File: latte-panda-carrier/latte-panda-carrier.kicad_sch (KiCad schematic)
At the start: 6 parts

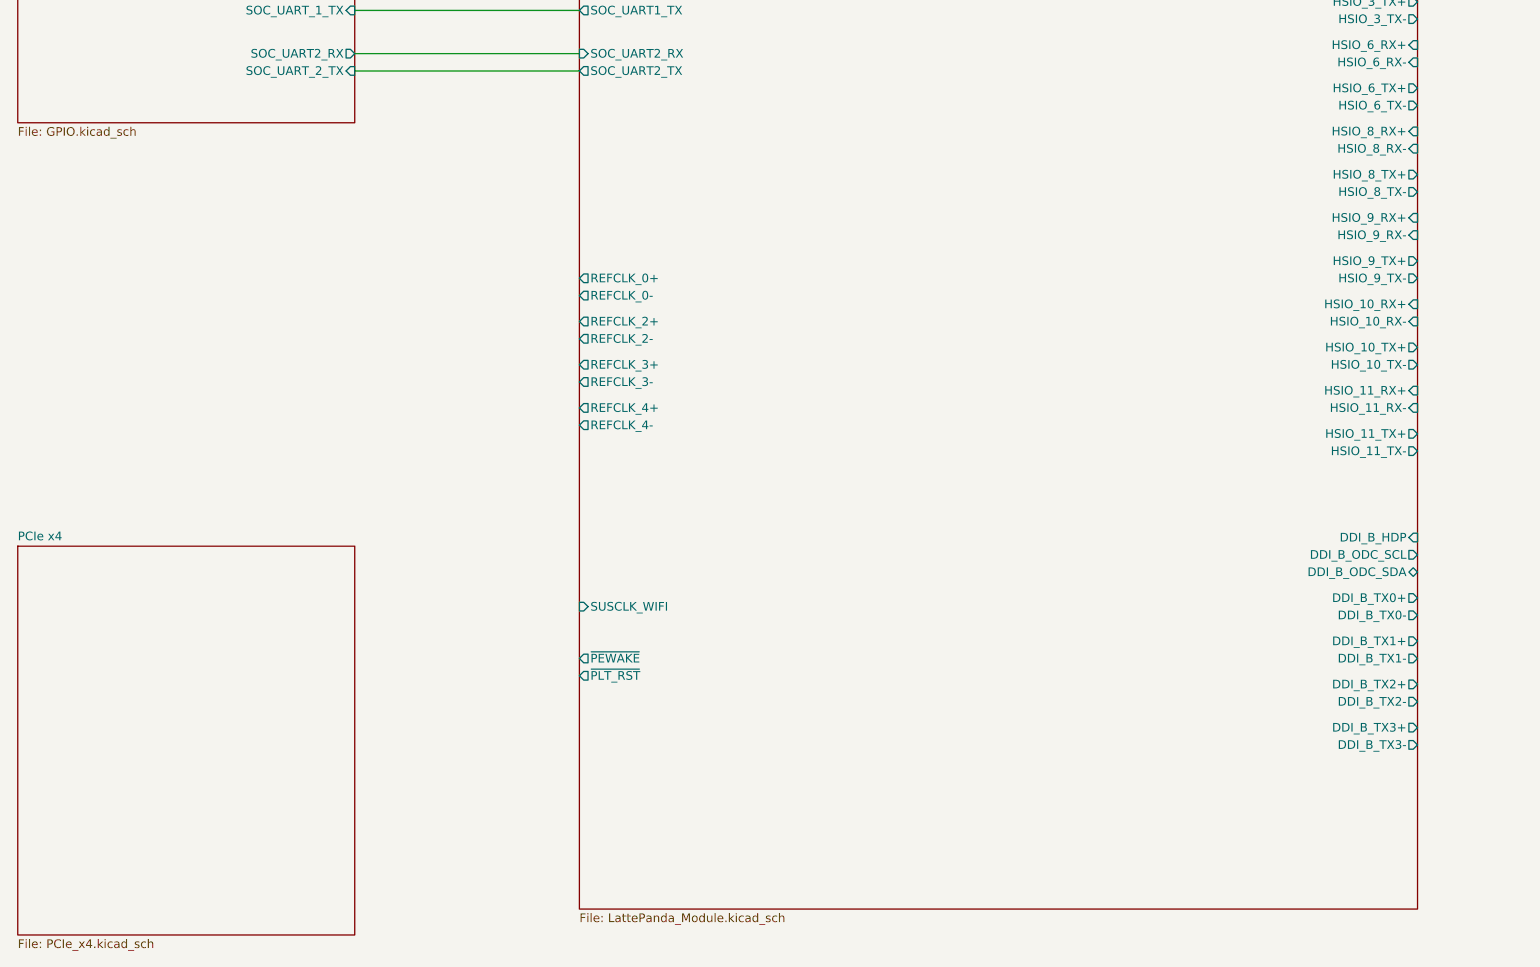
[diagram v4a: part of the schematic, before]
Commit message: 140.2
Add PCIe x4 connector. Instructor left one ERC problem, but I left it
unresolved, as ignored with a comment, as the course will not be routing it.
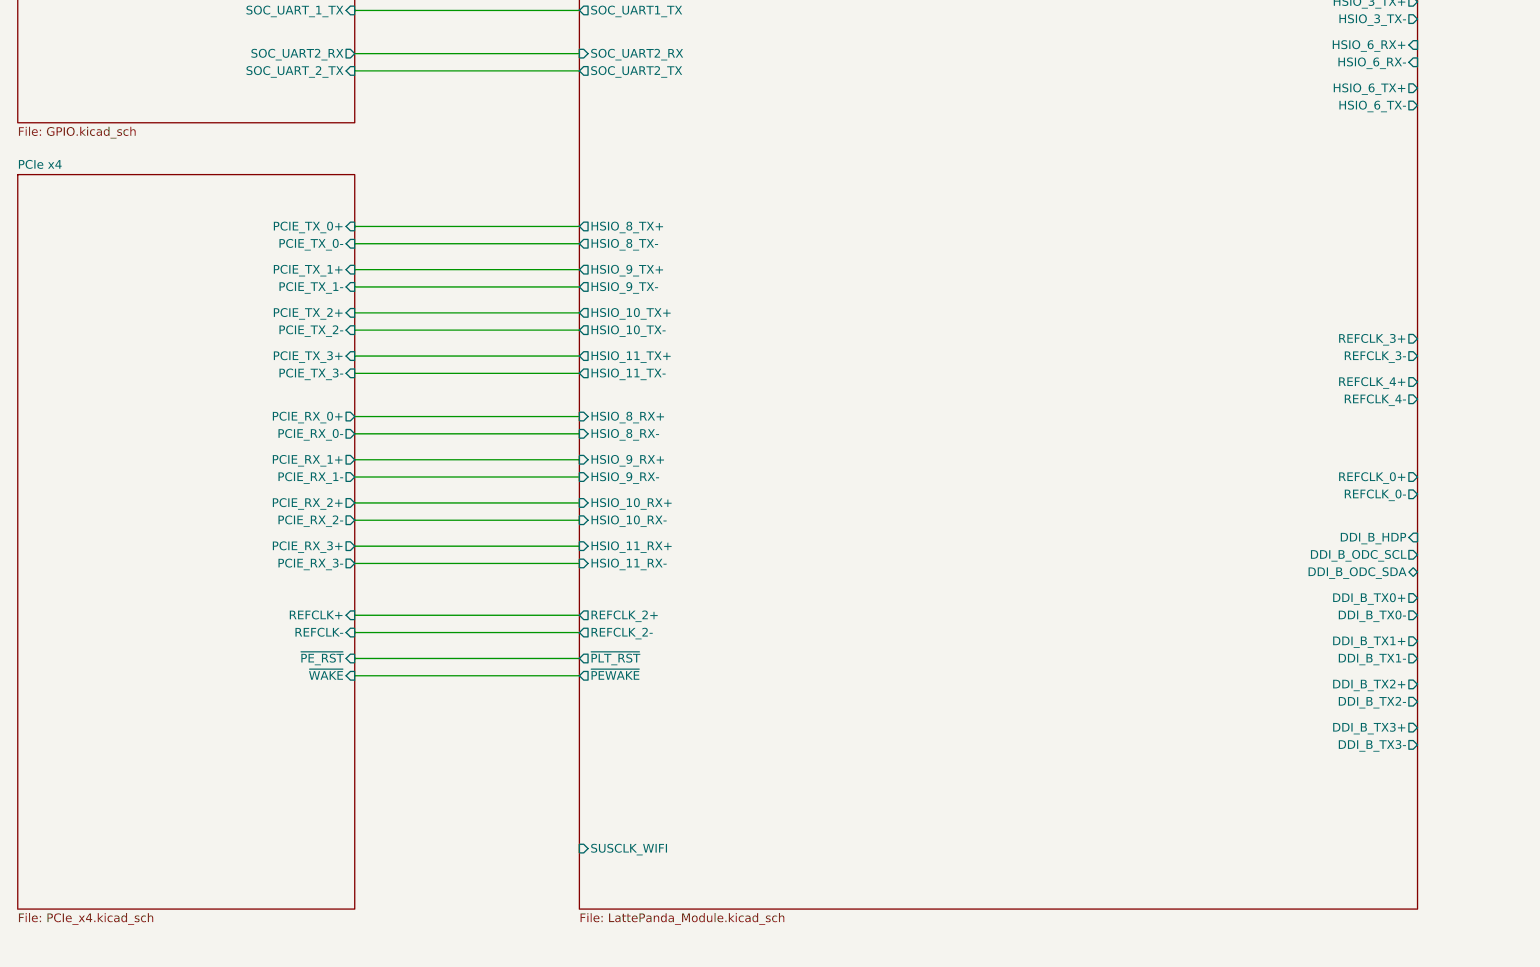
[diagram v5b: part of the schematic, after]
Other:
- sheet PCIe x4 ports: added PCIE_RX_0+, PCIE_RX_0-, PCIE_RX_1+, PCIE_RX_1-, PCIE_RX_2+, PCIE_RX_2-, PCIE_RX_3+, PCIE_RX_3-, PCIE_TX_0+, PCIE_TX_0-, PCIE_TX_1+, PCIE_TX_1-, PCIE_TX_2+, PCIE_TX_2-, PCIE_TX_3+, PCIE_TX_3-, REFCLK+, REFCLK-, ~{PE_RST}, ~{WAKE}; removed none

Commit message: 150
Add gigabit ethernet.
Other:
- sheet Ethernet ports: added GbE_PCIe_CLK+, GbE_PCIe_CLK-, GbE_PCIe_RX+, GbE_PCIe_RX-, GbE_PCIe_TX+, GbE_PCIe_TX-, ~{PLT_RST}; removed none
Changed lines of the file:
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@@
+	(wire
+		(pts
+			(xy 340.36 97.79) (xy 381 97.79)
+		)
+		(stroke
+			(width 0)
+			(type default)
+		)
+	)
 	(wire
 		(pts
@@
 	(wire
 		(pts
+			(xy 340.36 107.95) (xy 381 107.95)
+		)
+		(stroke
+			(width 0)
+			(type default)
+		)
+	)
+	(wire
+		(pts
 			(xy 184.15 167.64) (xy 217.17 167.64)
 		)
@@
 	(wire
 		(pts
+			(xy 375.92 87.63) (xy 381 87.63)
+		)
+		(stroke
+			(width 0)
+			(type default)
+		)
+	)
+	(wire
+		(pts
 			(xy 184.15 280.67) (xy 217.17 280.67)
 		)
@@
 	(wire
 		(pts
+			(xy 340.36 105.41) (xy 381 105.41)
+		)
+		(stroke
+			(width 0)
+			(type default)
+		)
+	)
+	(wire
+		(pts
 			(xy 184.15 72.39) (xy 217.17 72.39)
 		)
@@
 	(wire
 		(pts
+			(xy 340.36 93.98) (xy 381 93.98)
+		)
+		(stroke
+			(width 0)
+			(type default)
+		)
+	)
+	(wire
+		(pts
 			(xy 184.15 325.12) (xy 217.17 325.12)
 		)
@@
 	(wire
 		(pts
+			(xy 340.36 100.33) (xy 381 100.33)
+		)
+		(stroke
+			(width 0)
+			(type default)
+		)
+	)
+	(wire
+		(pts
 			(xy 184.15 187.96) (xy 217.17 187.96)
 		)
@@
 	(wire
 		(pts
+			(xy 340.36 91.44) (xy 381 91.44)
+		)
+		(stroke
+			(width 0)
+			(type default)
+		)
+	)
+	(wire
+		(pts
 			(xy 184.15 163.83) (xy 217.17 163.83)
 		)
@@
 			(width 0)
 			(type default)
+		)
+	)
+	(label "~{PLT_RST}"
+		(at 375.92 87.63 180)
+		(effects
+			(font
+				(size 1.27 1.27)
+			)
+			(justify right bottom)
 		)
 	)
@@
 			)
 		)
+		(pin "GbE_PCIe_CLK+" input
+			(at 381 107.95 180)
+			(effects
+				(font
+					(size 1.27 1.27)
+				)
+				(justify left)
+			)
+		)
+		(pin "GbE_PCIe_CLK-" input
+			(at 381 105.41 180)
+			(effects
+				(font
+					(size 1.27 1.27)
+				)
+				(justify left)
+			)
+		)
+		(pin "GbE_PCIe_RX+" output
+			(at 381 100.33 180)
+			(effects
+				(font
+					(size 1.27 1.27)
+				)
+				(justify left)
+			)
+		)
+		(pin "GbE_PCIe_RX-" output
+			(at 381 97.79 180)
+			(effects
+				(font
+					(size 1.27 1.27)
+				)
+				(justify left)
+			)
+		)
+		(pin "GbE_PCIe_TX+" input
+			(at 381 93.98 180)
+			(effects
+				(font
+					(size 1.27 1.27)
+				)
+				(justify left)
+			)
+		)
+		(pin "GbE_PCIe_TX-" input
+			(at 381 91.44 180)
+			(effects
+				(font
+					(size 1.27 1.27)
+				)
+				(justify left)
+			)
+		)
+		(pin "~{PLT_RST}" input
+			(at 381 87.63 180)
+			(effects
+				(font
+					(size 1.27 1.27)
+				)
+				(justify left)
+			)
+		)
 		(instances
 			(project "latte-panda-carrier"
@@
 		)
 		(pin "HSIO_6_RX+" input
-			(at 340.36 234.95 0)
+			(at 340.36 97.79 0)
 			(effects
 				(font
@@
 		)
 		(pin "HSIO_6_RX-" input
-			(at 340.36 237.49 0)
+			(at 340.36 100.33 0)
 			(effects
 				(font
@@
 		)
 		(pin "HSIO_6_TX+" output
-			(at 340.36 241.3 0)
+			(at 340.36 91.44 0)
 			(effects
 				(font
@@
 		)
 		(pin "HSIO_6_TX-" output
-			(at 340.36 243.84 0)
+			(at 340.36 93.98 0)
 			(effects
 				(font
@@
 		)
 		(pin "REFCLK_4+" output
-			(at 340.36 284.48 0)
+			(at 340.36 107.95 0)
 			(effects
 				(font
@@
 		)
 		(pin "REFCLK_4-" output
-			(at 340.36 287.02 0)
-			(effects
-				(font
+			(at 340.36 105.41 0)
+			(effects
+				(font

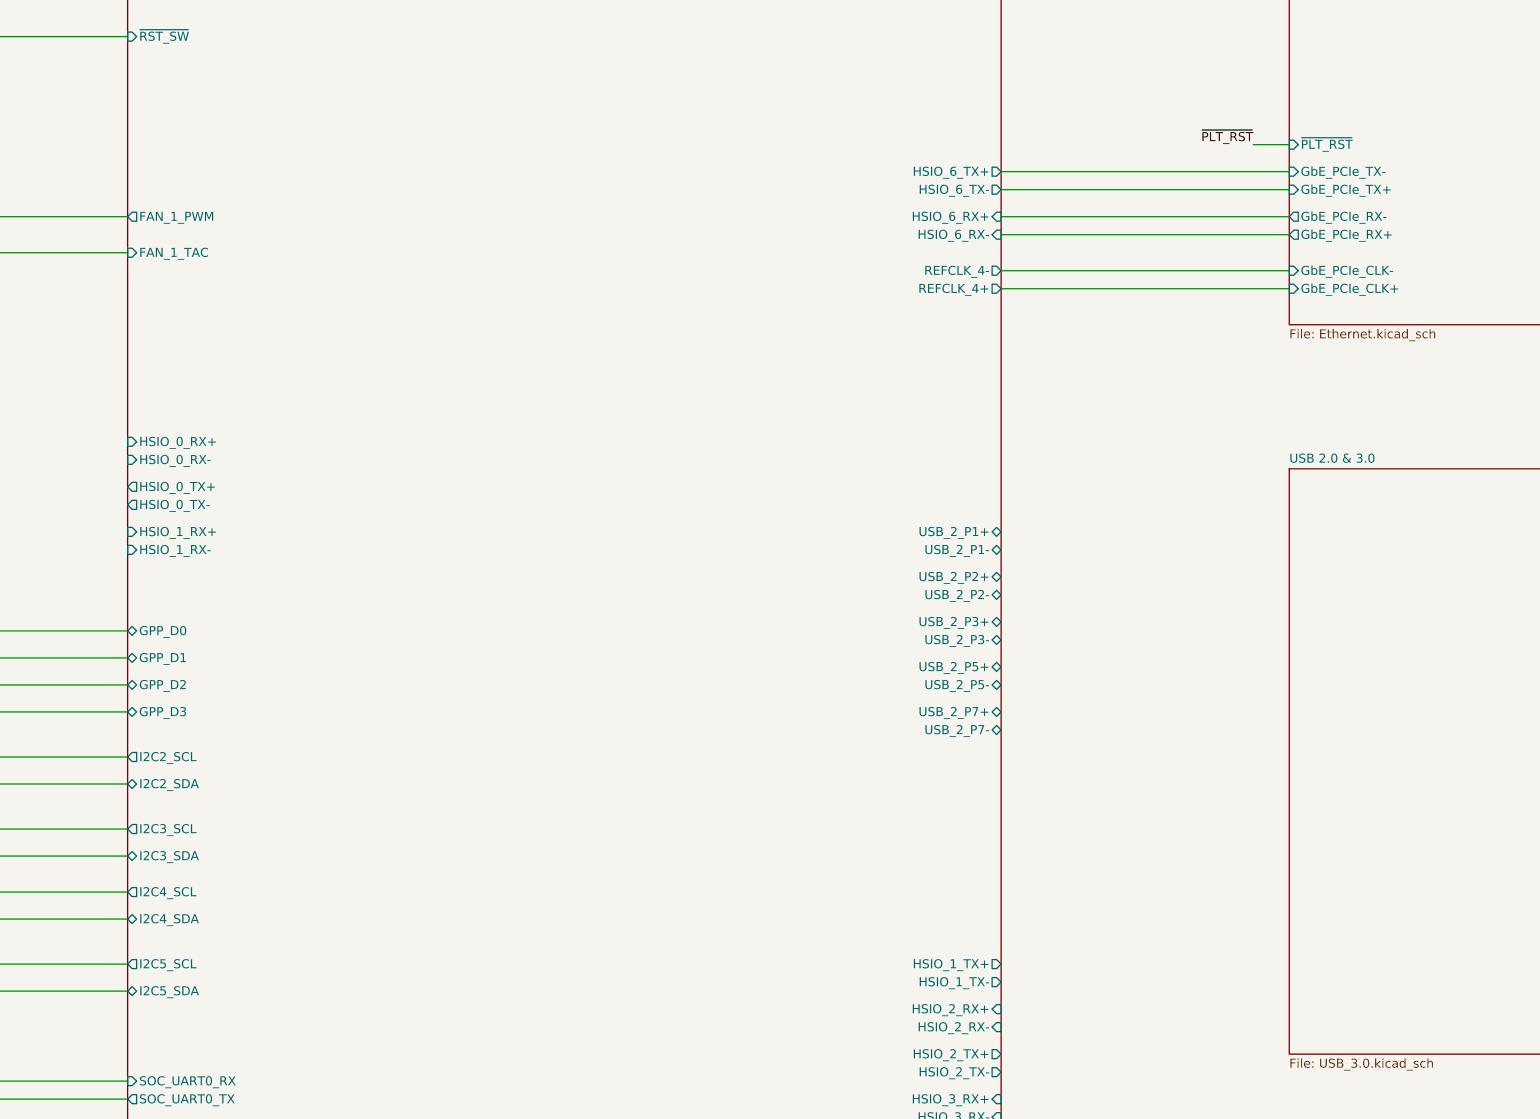
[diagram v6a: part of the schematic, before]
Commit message: 160.2
Sheet pins for the USB. Also fix some labels.
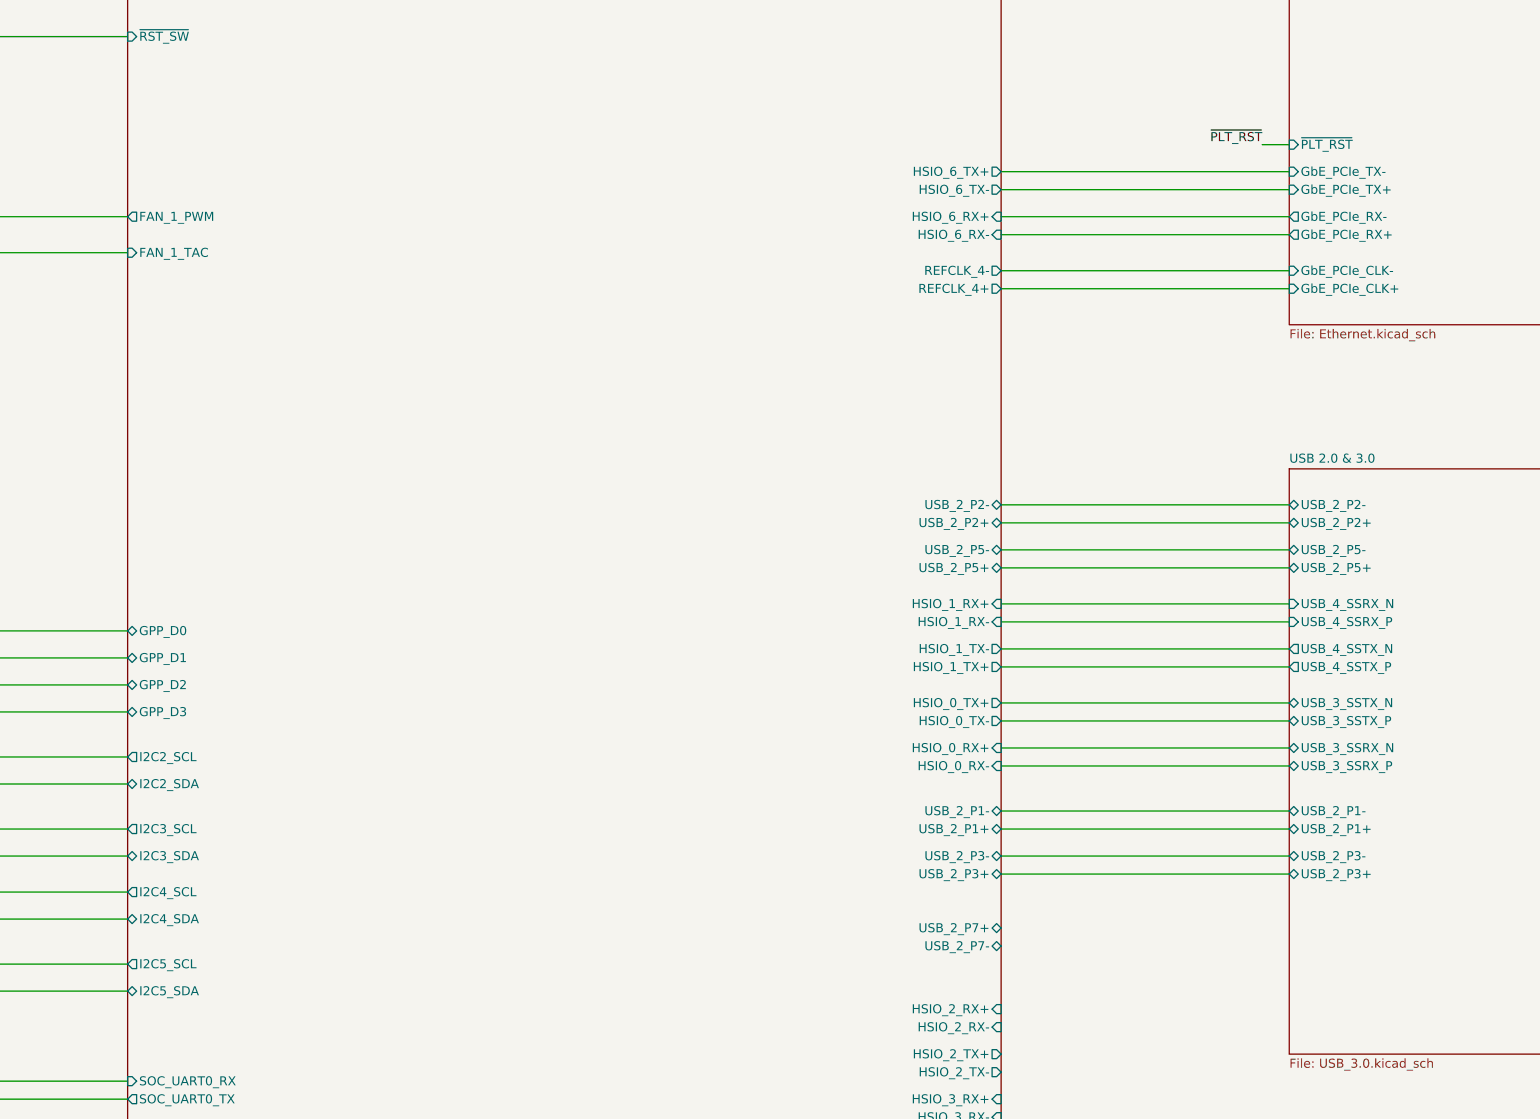
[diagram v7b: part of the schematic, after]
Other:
- sheet USB 2.0 & 3.0 ports: added USB_2_P1+, USB_2_P1-, USB_2_P2+, USB_2_P2-, USB_2_P3+, USB_2_P3-, USB_2_P5+, USB_2_P5-, USB_3_SSRX_N, USB_3_SSRX_P, USB_3_SSTX_N, USB_3_SSTX_P, USB_4_SSRX_N, USB_4_SSRX_P, USB_4_SSTX_N, USB_4_SSTX_P; removed none
